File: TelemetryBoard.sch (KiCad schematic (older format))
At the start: 43 parts, among them J2 Conn_01x02, J3 Micro_SD_Card_Det, J4 Conn_01x04, J5 Conn_01x04, J6 Conn_02x08_Odd_Even, J7 Conn_02x15_Odd_Even, J8 Conn_02x10_Odd_Even, J9 Conn_02x17_Odd_Even, U2 ADM3055E, U3 PQMC3-Dx-Sx-S, U4 CDSOT23-T24CAN

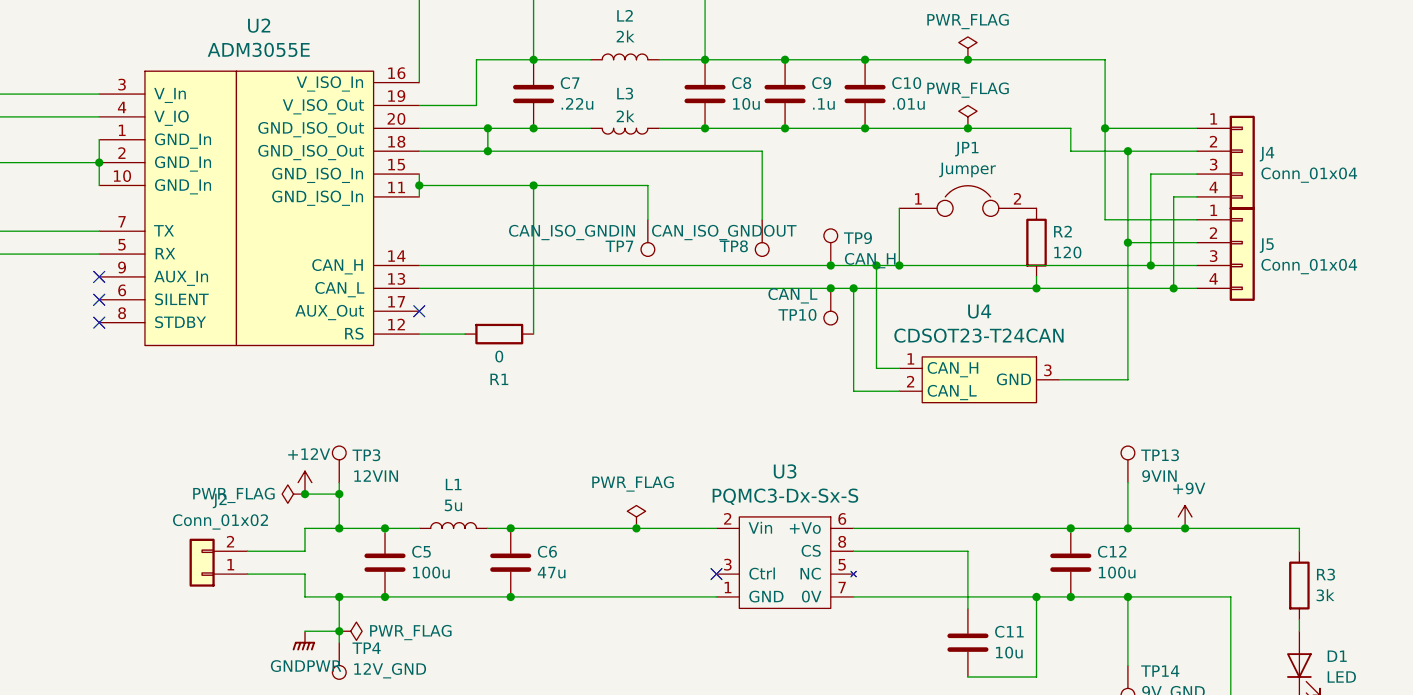
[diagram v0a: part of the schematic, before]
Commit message: Changes name of molex Power and CAN connectors to be more meaningful
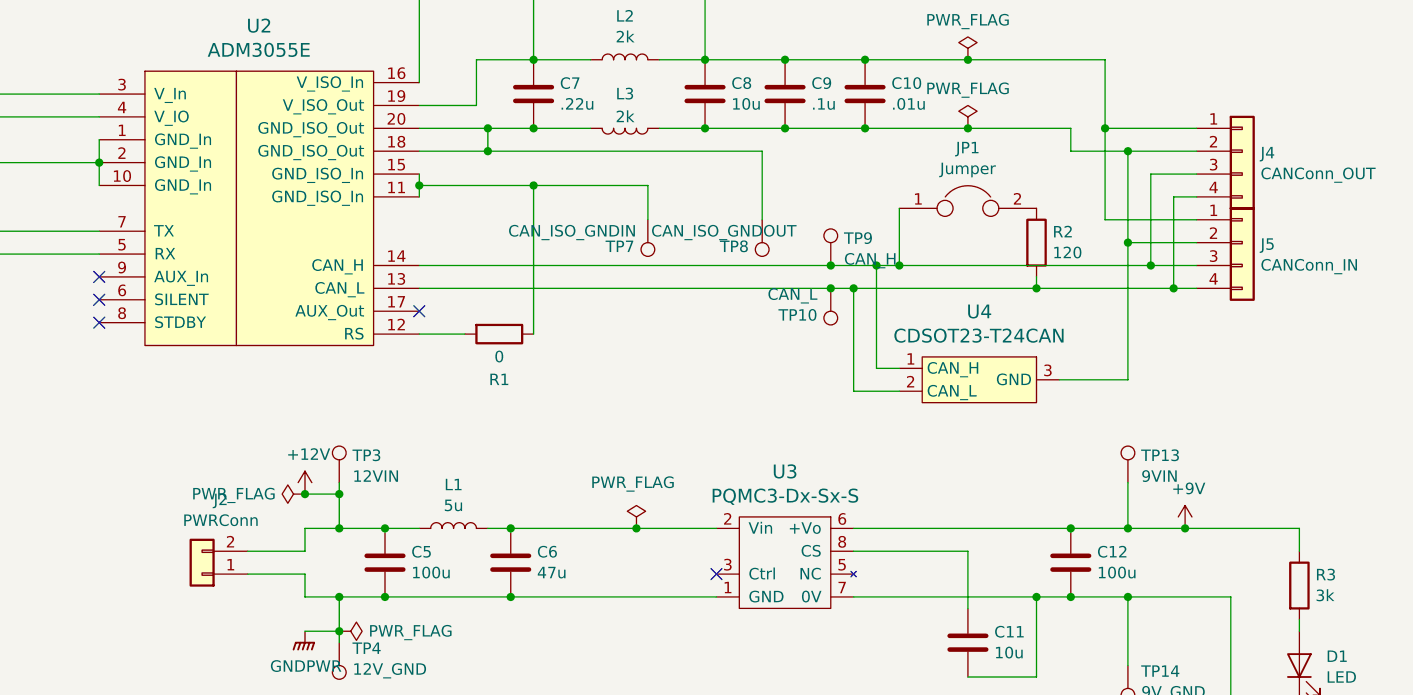
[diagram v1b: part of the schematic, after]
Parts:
- J2: value Conn_01x02 -> PWRConn
- J4: value Conn_01x04 -> CANConn_OUT
- J5: value Conn_01x04 -> CANConn_IN
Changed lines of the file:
@@
 P 10600 2600
 F 0 "J5" H 10680 2592 50  0000 L CNN
-F 1 "Conn_01x04" H 10680 2501 50  0000 L CNN
+F 1 "CANConn_IN" H 10680 2501 50  0000 L CNN
 F 2 "Connector_Molex:Molex_Micro-Fit_3.0_43650-0415_1x04_P3.00mm_Vertical" H 10600 2600 50  0001 C CNN
 F 3 "~" H 10600 2600 50  0001 C CNN
@@
 P 10600 2200
 F 0 "J4" H 10680 2192 50  0000 L CNN
-F 1 "Conn_01x04" H 10680 2101 50  0000 L CNN
+F 1 "CANConn_OUT" H 10680 2101 50  0000 L CNN
 F 2 "Connector_Molex:Molex_Micro-Fit_3.0_43650-0415_1x04_P3.00mm_Vertical" H 10600 2200 50  0001 C CNN
 F 3 "~" H 10600 2200 50  0001 C CNN
@@
 P 6050 4050
 F 0 "J2" H 5968 3725 50  0000 C CNN
-F 1 "Conn_01x02" H 5968 3816 50  0000 C CNN
+F 1 "PWRConn" H 5968 3816 50  0000 C CNN
 F 2 "Connector_Molex:Molex_Micro-Fit_3.0_43650-0215_1x02_P3.00mm_Vertical" H 6050 4050 50  0001 C CNN
 F 3 "~" H 6050 4050 50  0001 C CNN
